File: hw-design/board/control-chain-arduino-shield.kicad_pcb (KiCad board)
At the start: 2 copper layers, 68.6 x 53.3 mm, 8 parts, among them P1 Power, P2 Analog, P3 Digital, P4 Digital, P5 CONN_1, P6 CONN_1, P7 CONN_1, P8 CONN_1

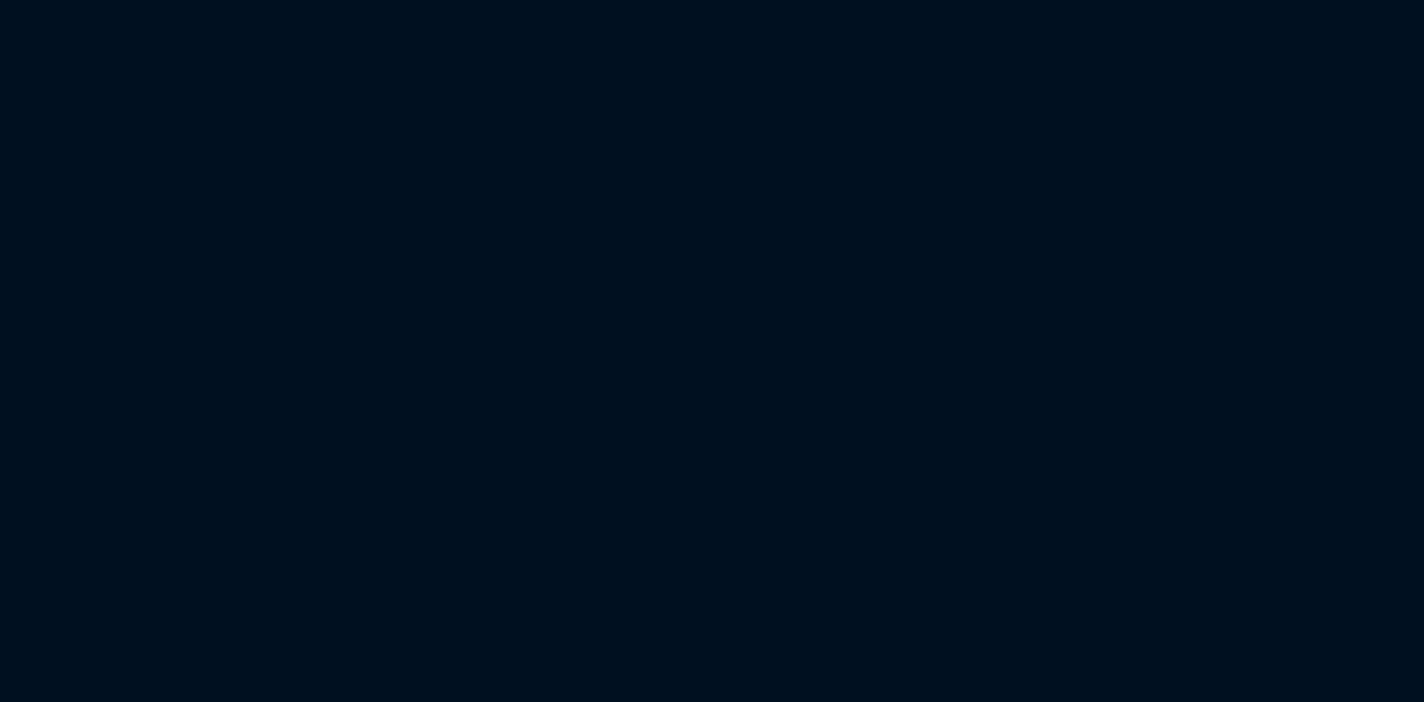
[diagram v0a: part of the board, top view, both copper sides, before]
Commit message: pcb: importing netlist
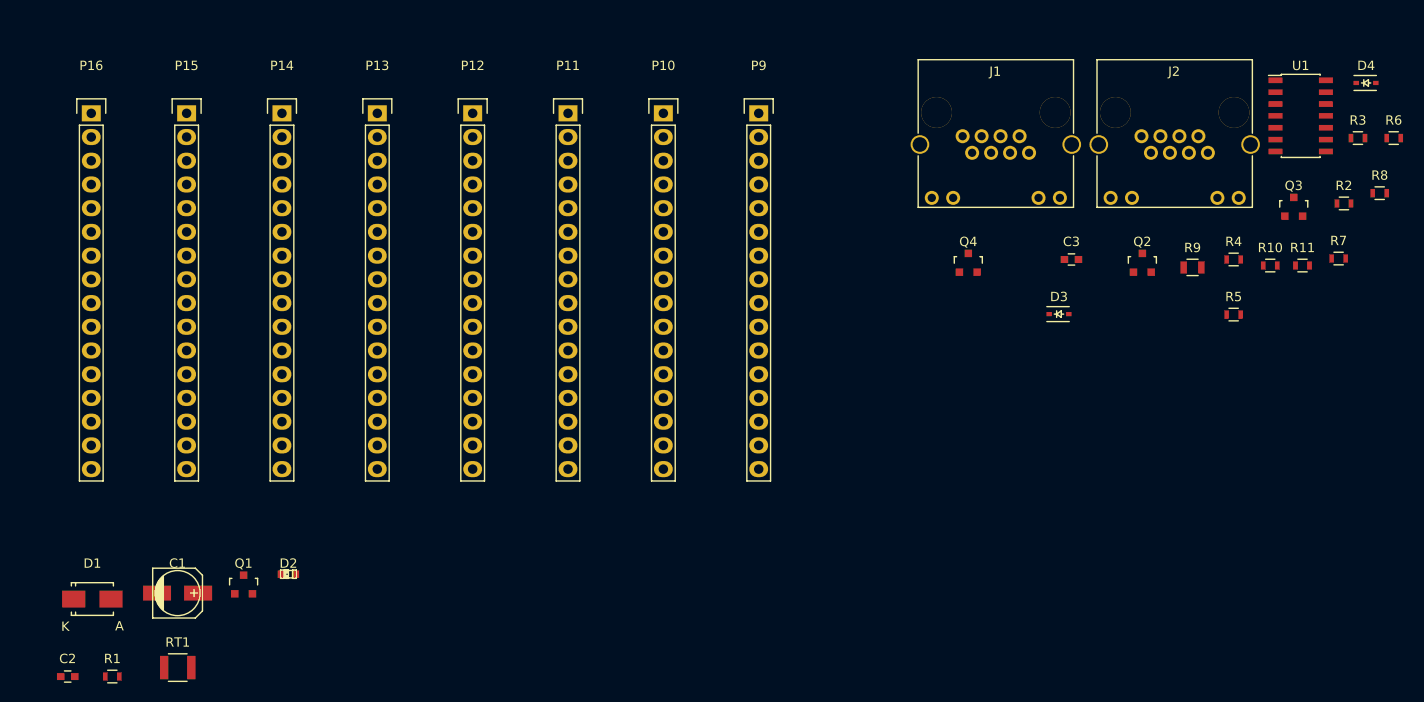
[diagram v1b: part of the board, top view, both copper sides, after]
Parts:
- added C1: 10uF, Capacitors_SMD:c_elec_5x5.3, F.Cu at (231.6, 139.6)
- added C2: 100nF, Capacitors_SMD:C_0603, F.Cu at (219.9, 148.5)
- added C3: 100nF X7R, Capacitors_SMD:C_0603, F.Cu at (327.4, 103.9)
- added D1: CGRA4007-G, Diodes_SMD:Diode-SMA_Standard, F.Cu at (222.5, 140.2)
- added D2: LED, LEDs:LED-0603, F.Cu at (243.5, 137.6)
- added D3: 1N4148, Diodes_SMD:SOD-323, F.Cu at (326.0, 109.7)
- added D4: 1N4148, Diodes_SMD:SOD-323, F.Cu at (358.9, 85.0)
- added J1: CC_INPUT, Connect:RJHSE538X, F.Cu at (315.7, 90.7)
- added J2: CC_OUTPUT, Connect:RJHSE538X, F.Cu at (334.8, 90.7)
- added P10: CONN_01X16, Pin_Headers:Pin_Header_Straight_1x16, F.Cu at (283.7, 88.2)
- added P11: CONN_01X16, Pin_Headers:Pin_Header_Straight_1x16, F.Cu at (273.4, 88.2)
- added P12: CONN_01X16, Pin_Headers:Pin_Header_Straight_1x16, F.Cu at (263.2, 88.2)
- added P13: CONN_01X16, Pin_Headers:Pin_Header_Straight_1x16, F.Cu at (253.0, 88.2)
- added P14: CONN_01X16, Pin_Headers:Pin_Header_Straight_1x16, F.Cu at (242.8, 88.2)
- added P15: CONN_01X16, Pin_Headers:Pin_Header_Straight_1x16, F.Cu at (232.6, 88.2)
- added P16: CONN_01X16, Pin_Headers:Pin_Header_Straight_1x16, F.Cu at (222.4, 88.2)
- added P9: CONN_01X16, Pin_Headers:Pin_Header_Straight_1x16, F.Cu at (293.9, 88.2)
- added Q1: 2N7002, Housings_SOT-23_SOT-143_TSOT-6:SOT-23, F.Cu at (238.7, 138.7)
- added Q2: 2N7002, Housings_SOT-23_SOT-143_TSOT-6:SOT-23, F.Cu at (334.9, 104.2)
- added Q3: 2N7002, Housings_SOT-23_SOT-143_TSOT-6:SOT-23, F.Cu at (351.2, 98.2)
- added Q4: IRFML8244TRPBF, Housings_SOT-23_SOT-143_TSOT-6:SOT-23, F.Cu at (316.3, 104.2)
- added R1: 820R, Resistors_SMD:R_0603, F.Cu at (224.6, 148.5)
- added R10: 10k, Resistors_SMD:R_0603, F.Cu at (348.6, 104.5)
- added R11: 10K, Resistors_SMD:R_0603, F.Cu at (352.1, 104.5)
- added R2: 820R, Resistors_SMD:R_0603, F.Cu at (356.5, 97.9)
- added R3: 820R, Resistors_SMD:R_0603, F.Cu at (358.0, 90.9)
- added R4: 820R, Resistors_SMD:R_0603, F.Cu at (344.7, 103.9)
- added R5: 820R, Resistors_SMD:R_0603, F.Cu at (344.7, 109.8)
- added R6: 10k, Resistors_SMD:R_0603, F.Cu at (361.9, 90.9)
- added R7: 10k, Resistors_SMD:R_0603, F.Cu at (356.0, 103.8)
- added R8: 10k, Resistors_SMD:R_0603, F.Cu at (360.4, 96.8)
- added R9: 100R, Resistors_SMD:R_0805, F.Cu at (340.3, 104.7)
- added RT1: PTC_FUSE, Resistors_SMD:R_1210, F.Cu at (231.7, 147.6)
- added U1: ISL83491, Housings_SOIC:SOIC-14_3.9x8.7mm_Pitch1.27mm, F.Cu at (351.9, 88.5)
- P5, P6, P7, P8: value CONN_1 -> Hole
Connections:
- net /0(Rx) renamed IO7
- net /1(Tx) renamed IO6
- net /10(**/SS) renamed AREF
- net /13(SCK) renamed IO12/MISO
- net /2 renamed IO5
- net /3(**) renamed IO4
- net /4 renamed IO3
- net /A2 renamed AD3
- net /A3 renamed AD2
- net /AREF renamed IO10/SS
- net /IOREF renamed IOREF
- net /Reset renamed RESET
- P1 pad 6: GND -> GNDD
- P1 pad 7: GND -> GNDD
- P1 pad 8: /Vin -> +9V
- P2 pad 1: /A0 -> AD5/SCL
- P2 pad 2: /A1 -> AD4/SDA
- P2 pad 5: /A4(SDA) -> AD1
- P2 pad 6: /A5(SCL) -> AD0
- P3 pad 1: /A5(SCL) -> IO8
- P3 pad 10: /8 -> AD5/SCL
- P3 pad 2: /A4(SDA) -> IO9
- P3 pad 4: GND -> IO11/MOSI
- P3 pad 6: /12(MISO) -> IO13/SCK
- P3 pad 7: /11(**/MOSI) -> GNDD
- P3 pad 9: /9(**) -> AD4/SDA
- P4 pad 1: /7 -> IO0/RXD
- P4 pad 2: /6(**) -> IO1/TXD
- P4 pad 3: /5(**) -> IO2

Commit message: pcb: RJ45 connectors placed
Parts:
- moved J2 217.2 mm to (117.7, 92.8), turned to 90 degrees
- moved J1 199.4 mm to (117.7, 113.7), turned to 90 degrees
- moved D3 114.0 mm to (212.0, 112.5)
- moved D4 114.0 mm to (244.9, 87.8)
- moved Q3 114.0 mm to (237.2, 101.0)
- moved Q4 114.0 mm to (202.3, 107.0)
- moved R10 114.0 mm to (234.6, 107.3)
- moved R2 114.0 mm to (242.5, 100.7)
- moved R3 114.0 mm to (244.0, 93.7)
- moved R4 114.0 mm to (230.7, 106.7)
- moved R5 114.0 mm to (230.7, 112.6)
- moved R6 114.0 mm to (247.9, 93.7)
- moved R8 114.0 mm to (246.4, 99.6)
- moved R9 114.0 mm to (226.3, 107.5)
- moved C3 114.0 mm to (213.4, 106.7)
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
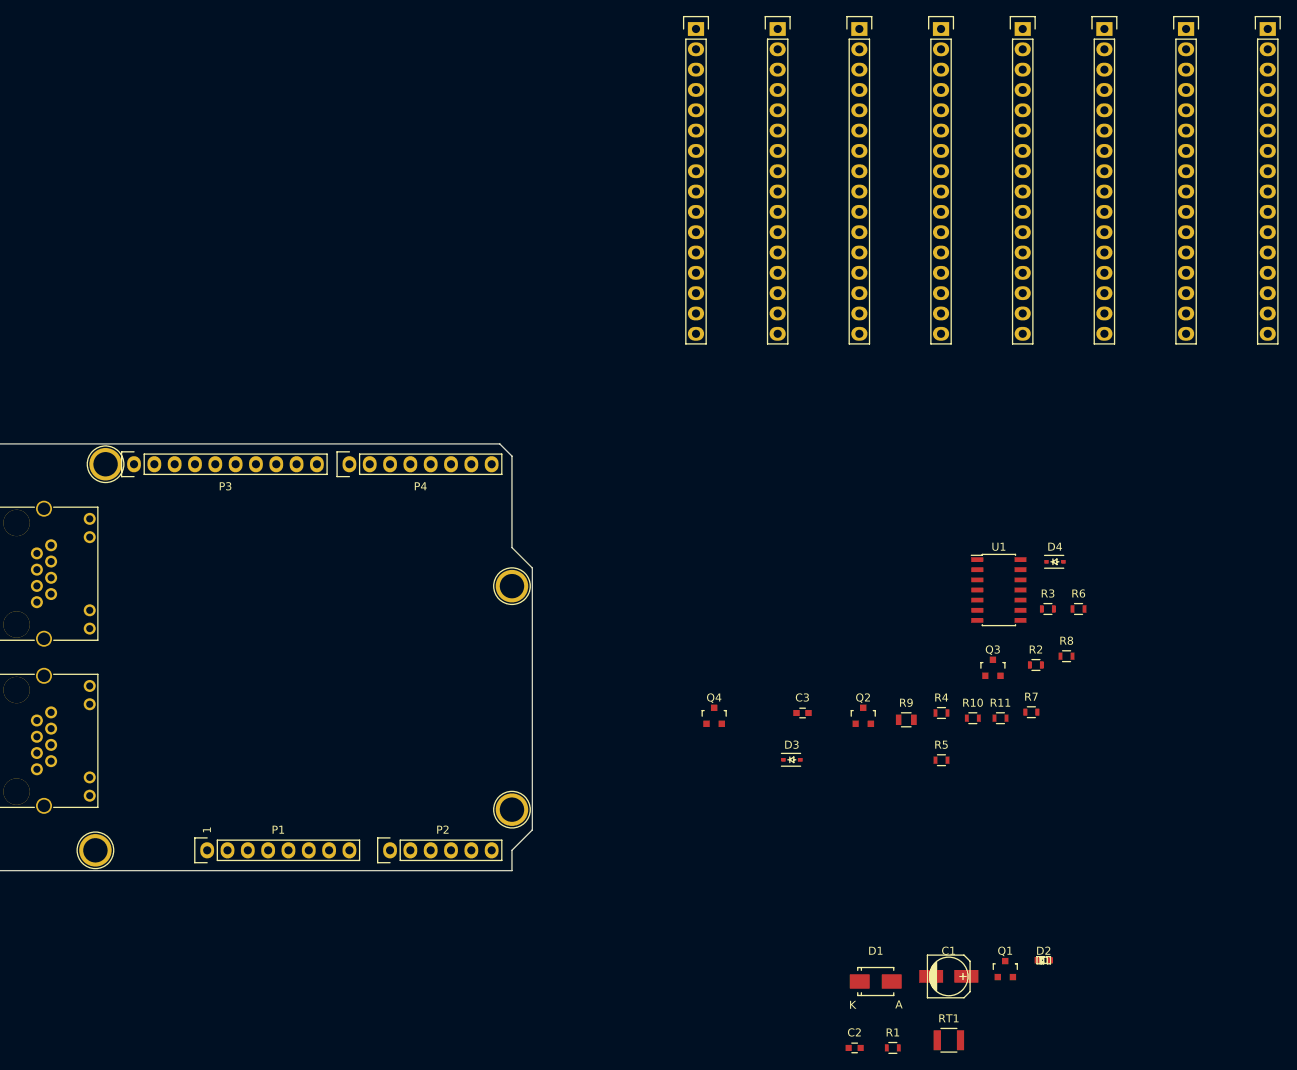
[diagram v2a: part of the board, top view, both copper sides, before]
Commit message: pcb: initial placement of components
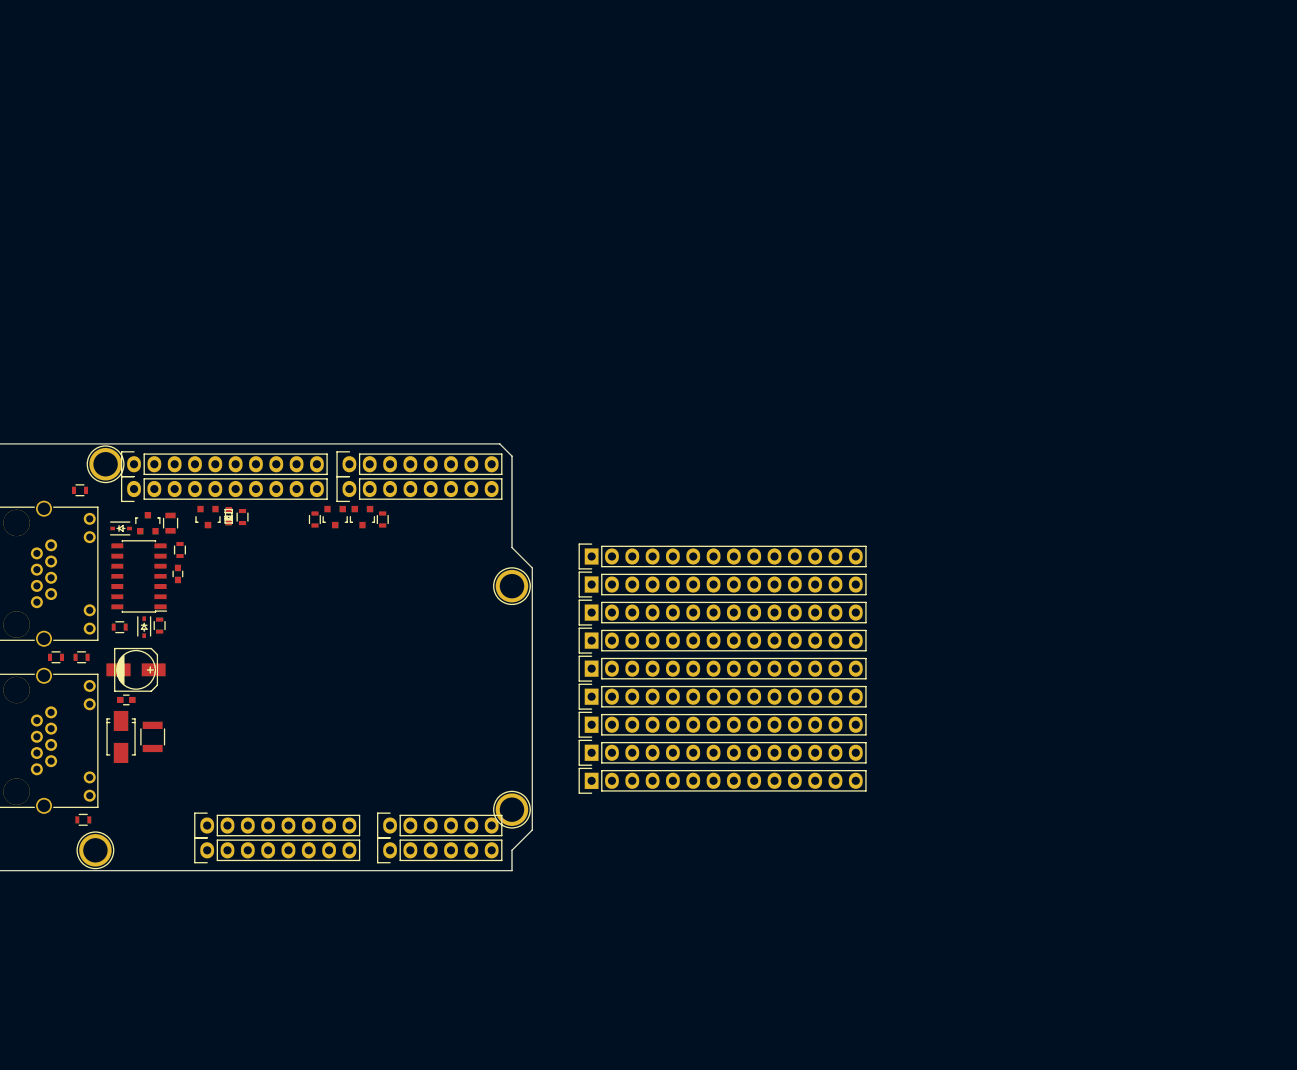
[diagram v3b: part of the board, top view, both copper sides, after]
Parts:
- added P17: ~, Pin_Headers:Pin_Header_Straight_1x14, F.Cu at (187.0, 108.1)
- added P18: ~, Pin_Headers:Pin_Header_Straight_1x14, F.Cu at (187.0, 111.6)
- added P19: ~, Pin_Headers:Pin_Header_Straight_1x14, F.Cu at (187.0, 115.1)
- added P20: ~, Pin_Headers:Pin_Header_Straight_1x14, F.Cu at (187.0, 87.1)
- added P21: ~, Pin_Headers:Pin_Header_Straight_1x14, F.Cu at (187.0, 101.1)
- P10: value CONN_01X16 -> Power; footprint Pin_Headers:Pin_Header_Straight_1x16 -> Socket_Arduino_Uno:Socket_Strip_Arduino_1x08
- P11: value CONN_01X16 -> Analog; footprint Pin_Headers:Pin_Header_Straight_1x16 -> Socket_Arduino_Uno:Socket_Strip_Arduino_1x06
- P12: value CONN_01X16 -> Digital; footprint Pin_Headers:Pin_Header_Straight_1x16 -> Socket_Arduino_Uno:Socket_Strip_Arduino_1x10
- P13: value CONN_01X16 -> Digital; footprint Pin_Headers:Pin_Header_Straight_1x16 -> Socket_Arduino_Uno:Socket_Strip_Arduino_1x08
- P14, P15, P16, P9: value CONN_01X16 -> ~; footprint Pin_Headers:Pin_Header_Straight_1x16 -> Pin_Headers:Pin_Header_Straight_1x14
- moved P10 157.8 mm to (138.9, 120.7)
- moved P11 133.7 mm to (161.8, 120.7)
- moved P12 125.1 mm to (129.8, 78.7)
- moved R3 123.4 mm to (123.4, 120.0), turned to 180 degrees
- moved R2 122.5 mm to (120.0, 99.7)
- moved P9 118.8 mm to (187.0, 104.6), turned to 90 degrees
- moved D2 116.0 mm to (141.6, 82.1), turned to 90 degrees
- moved Q1 114.6 mm to (139.0, 82.2), turned to 180 degrees
- moved D4 114.1 mm to (131.1, 95.9), turned to 270 degrees
- moved R8 111.6 mm to (135.5, 86.3), turned to 90 degrees
- moved R4 111.2 mm to (123.0, 78.8)
- moved R11 110.7 mm to (128.0, 95.9)
- moved C1 108.6 mm to (130.0, 101.3)
- moved R5 108.2 mm to (123.2, 99.7)
- moved U1 107.5 mm to (130.4, 89.6), turned to 180 degrees
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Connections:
- P10 pad 2: Net-(P10-Pad2) -> IOREF
- P10 pad 3: Net-(P10-Pad3) -> RESET
- P10 pad 4: Net-(P10-Pad4) -> +3V3
- P10 pad 5: Net-(P10-Pad5) -> +5V
- P10 pad 6: Net-(P10-Pad6) -> GNDD
- P10 pad 7: Net-(P10-Pad7) -> GNDD
- P10 pad 8: Net-(P10-Pad8) -> +9V
- P11 pad 1: Net-(P11-Pad1) -> AD5/SCL
- P11 pad 2: Net-(P11-Pad2) -> AD4/SDA
- P11 pad 3: Net-(P11-Pad3) -> AD3
- P11 pad 4: Net-(P11-Pad4) -> AD2
- P11 pad 5: Net-(P11-Pad5) -> AD1
- P11 pad 6: Net-(P11-Pad6) -> AD0
- P12 pad 1: Net-(P12-Pad1) -> IO8
- P12 pad 10: Net-(P12-Pad10) -> AD5/SCL
- P12 pad 2: Net-(P12-Pad2) -> IO9
- P12 pad 3: Net-(P12-Pad3) -> IO10/SS
- P12 pad 4: Net-(P12-Pad4) -> IO11/MOSI
- P12 pad 5: Net-(P12-Pad5) -> IO12/MISO
- P12 pad 6: Net-(P12-Pad6) -> IO13/SCK
- P12 pad 7: Net-(P12-Pad7) -> GNDD
- P12 pad 8: Net-(P12-Pad8) -> AREF
- P12 pad 9: Net-(P12-Pad9) -> AD4/SDA
- P13 pad 1: Net-(P13-Pad1) -> IO0/RXD
- P13 pad 2: Net-(P13-Pad2) -> IO1/TXD
- P13 pad 3: Net-(P13-Pad3) -> IO2
- P13 pad 4: Net-(P13-Pad4) -> IO3
- P13 pad 5: Net-(P13-Pad5) -> IO4
- P13 pad 6: Net-(P13-Pad6) -> IO5
- P13 pad 7: Net-(P13-Pad7) -> IO6
- P13 pad 8: Net-(P13-Pad8) -> IO7
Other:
- board text removed: "1"

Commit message: pcb: setting design rules
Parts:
- moved U1 0.97 mm to (129.4, 89.6)
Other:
- net class Default: clearance 0.2 -> 0.15; trace_width 0.25 -> 0.3048; via_drill 0.4 -> 0.3
- rule trace_clearance: 0.2 -> 0.15
- rule trace_min: 0.2 -> 0.2032
- rule via_min_size: 0.4 -> 0.6
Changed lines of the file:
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@@
   )
   (setup
-    (last_trace_width 0.25)
-    (trace_clearance 0.2)
+    (last_trace_width 0.3048)
+    (user_trace_width 0.2032)
+    (user_trace_width 0.254)
+    (user_trace_width 0.3048)
+    (user_trace_width 0.381)
+    (user_trace_width 0.508)
+    (user_trace_width 0.762)
+    (user_trace_width 1.27)
+    (user_trace_width 1.905)
+    (trace_clearance 0.15)
     (zone_clearance 0.508)
     (zone_45_only no)
-    (trace_min 0.2)
+    (trace_min 0.2032)
     (segment_width 0.15)
     (edge_width 0.15)
     (via_size 0.6)
-    (via_drill 0.4)
-    (via_min_size 0.4)
+    (via_drill 0.3)
+    (via_min_size 0.6)
     (via_min_drill 0.3)
-    (uvia_size 0.3)
-    (uvia_drill 0.1)
+    (user_via 0.6 0.3)
+    (user_via 0.75 0.375)
+    (user_via 0.9 0.45)
+    (uvia_size 0.0889)
+    (uvia_drill 0.0635)
     (uvias_allowed no)
-    (uvia_min_size 0.2)
-    (uvia_min_drill 0.1)
+    (uvia_min_size 0.06)
+    (uvia_min_drill 0.03)
     (pcb_text_width 0.3)
     (pcb_text_size 1.5 1.5)
@@
   (net 136 "Net-(P18-Pad14)")
   (net_class Default "This is the default net class."
-    (clearance 0.2)
-    (trace_width 0.25)
+    (clearance 0.15)
+    (trace_width 0.3048)
     (via_dia 0.6)
-    (via_drill 0.4)
-    (uvia_dia 0.3)
-    (uvia_drill 0.1)
+    (via_drill 0.3)
+    (uvia_dia 0.0889)
+    (uvia_drill 0.0635)
     (add_net +3V3)
     (add_net +5V)
@@
   )
   (module Housings_SOIC:SOIC-14_3.9x8.7mm_Pitch1.27mm (layer F.Cu)
-    (at 130.4036 89.5858 180)
+    (at 129.4384 89.6366 180)
     (descr "14-Lead Plastic Small Outline (SL) - Narrow, 3.90 mm Body [SOIC] (see Microchip Packaging Specification 00000049BS.pdf)")
     (tags "SOIC 1.27")
